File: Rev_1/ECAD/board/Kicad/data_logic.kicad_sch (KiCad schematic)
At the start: 5 parts

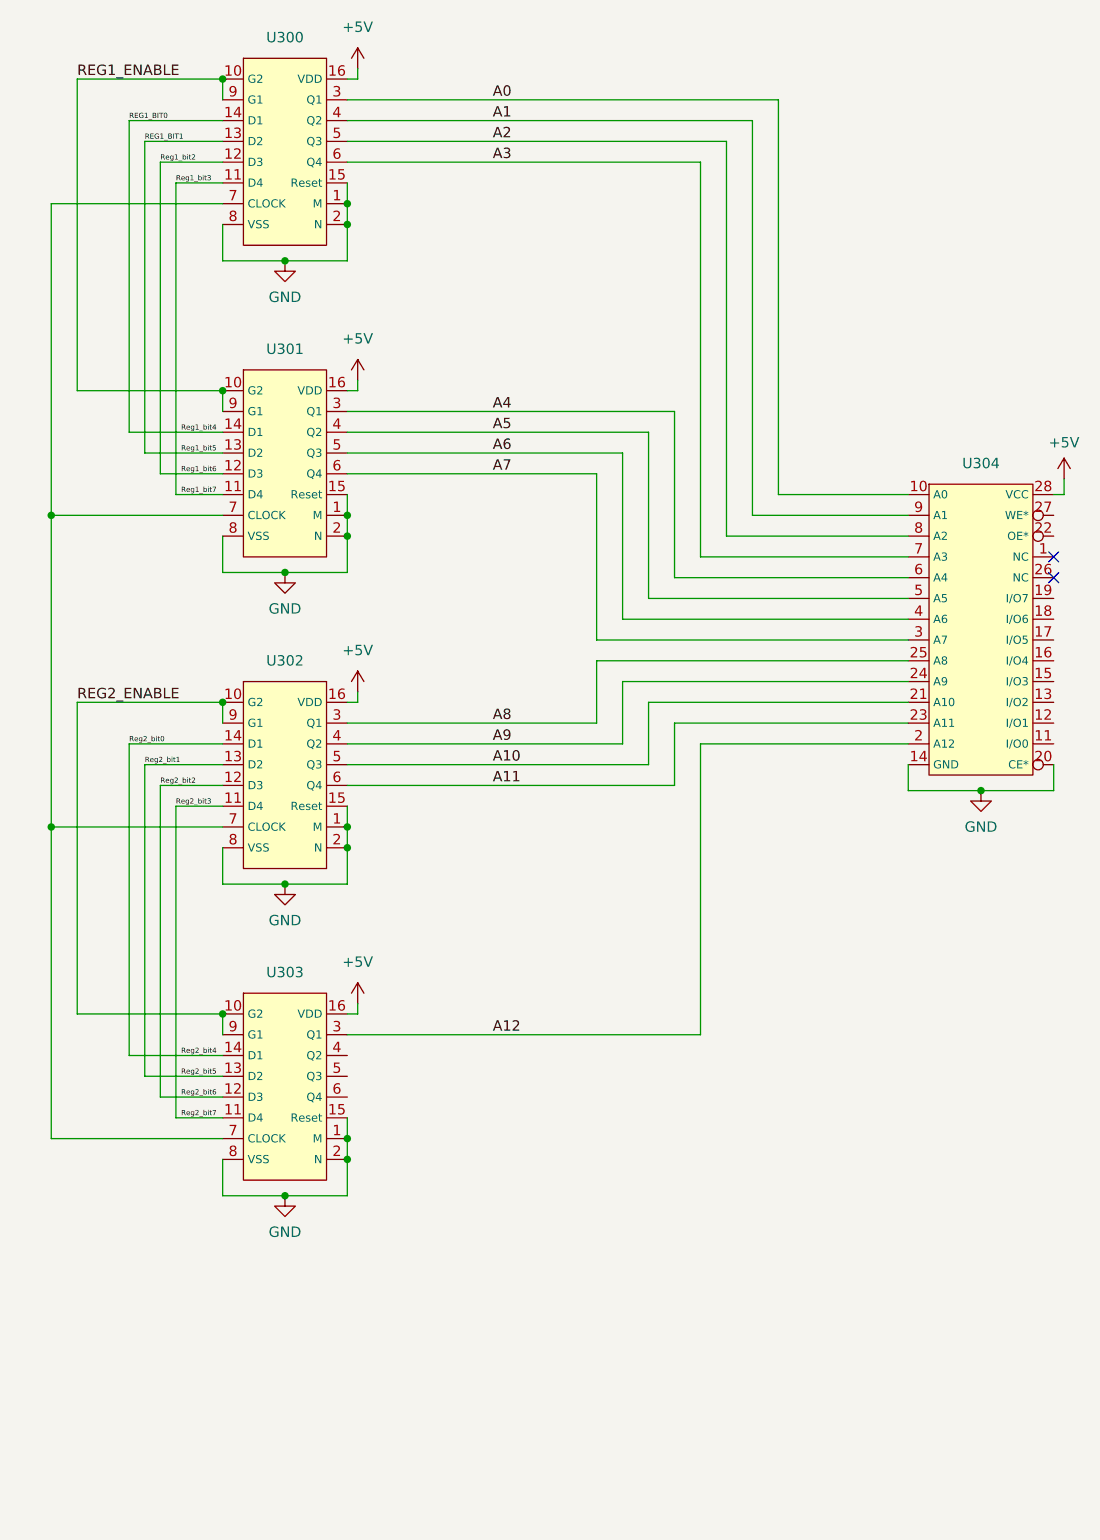
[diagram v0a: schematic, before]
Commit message: Updated net-name on Data Logic sheet
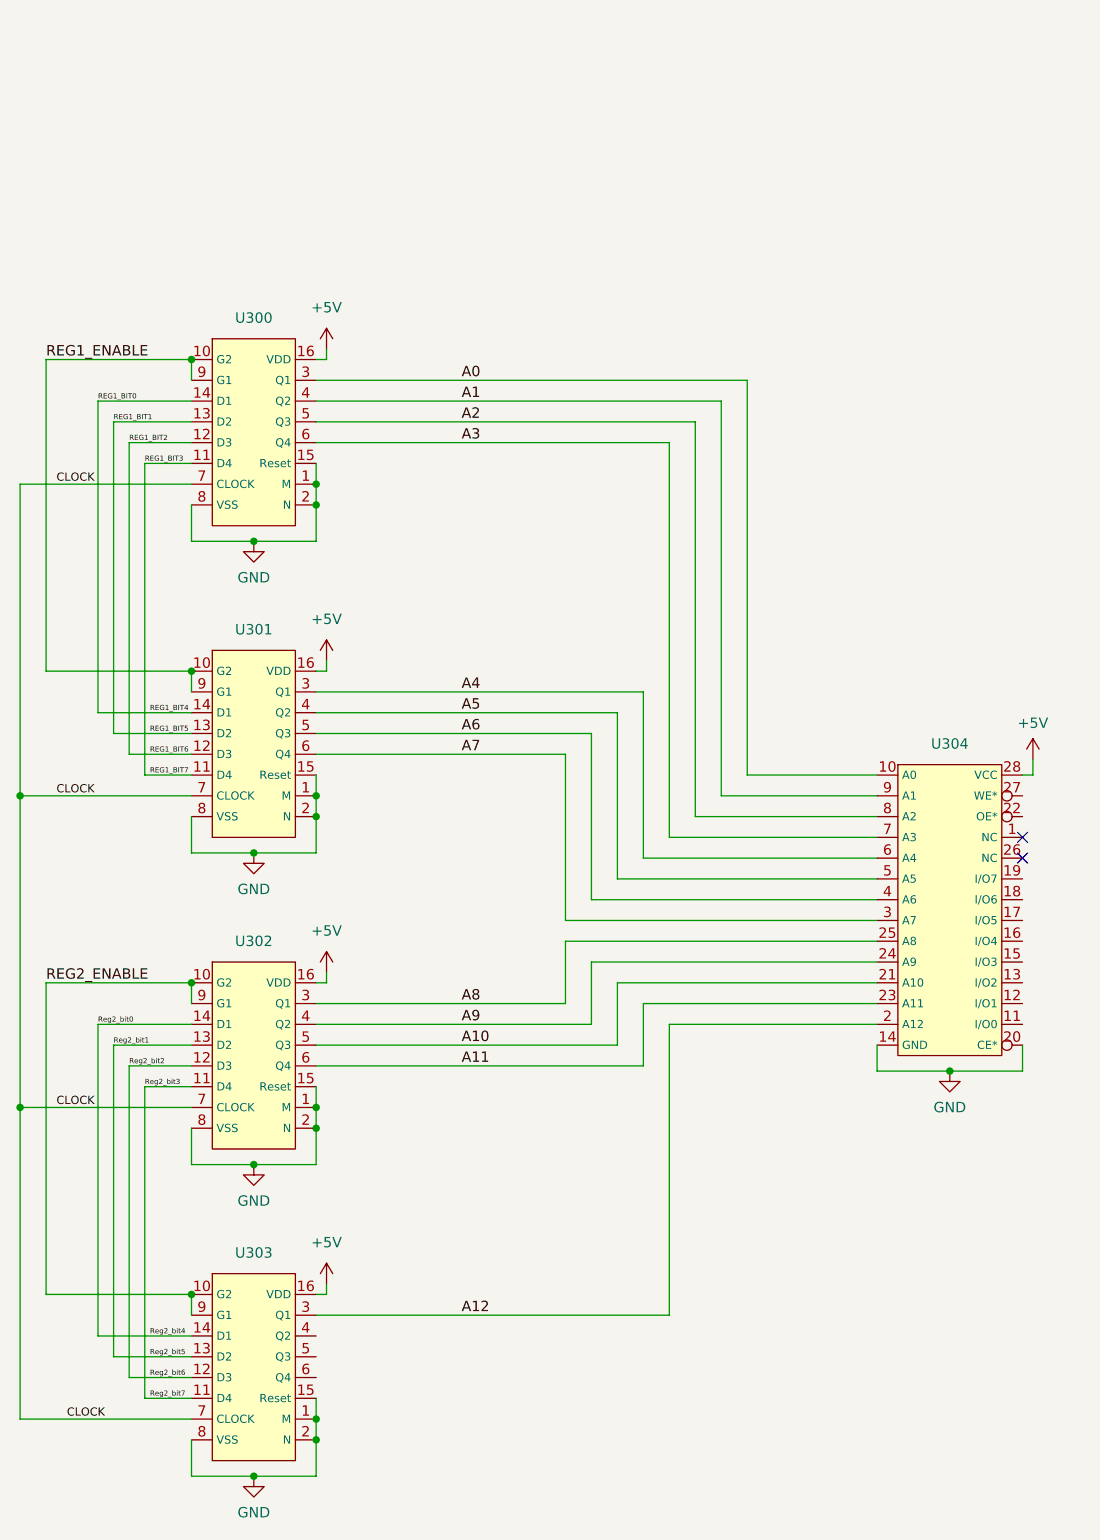
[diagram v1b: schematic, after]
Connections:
- net CLOCK: now reaches U300.7 (CLOCK), U301.7 (CLOCK), U302.7 (CLOCK), U303.7 (CLOCK)
- net Reg1_bit2 renamed REG1_BIT2
- net Reg1_bit3 renamed REG1_BIT3
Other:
- moved on the sheet: U300, U301, U302, U303, U304

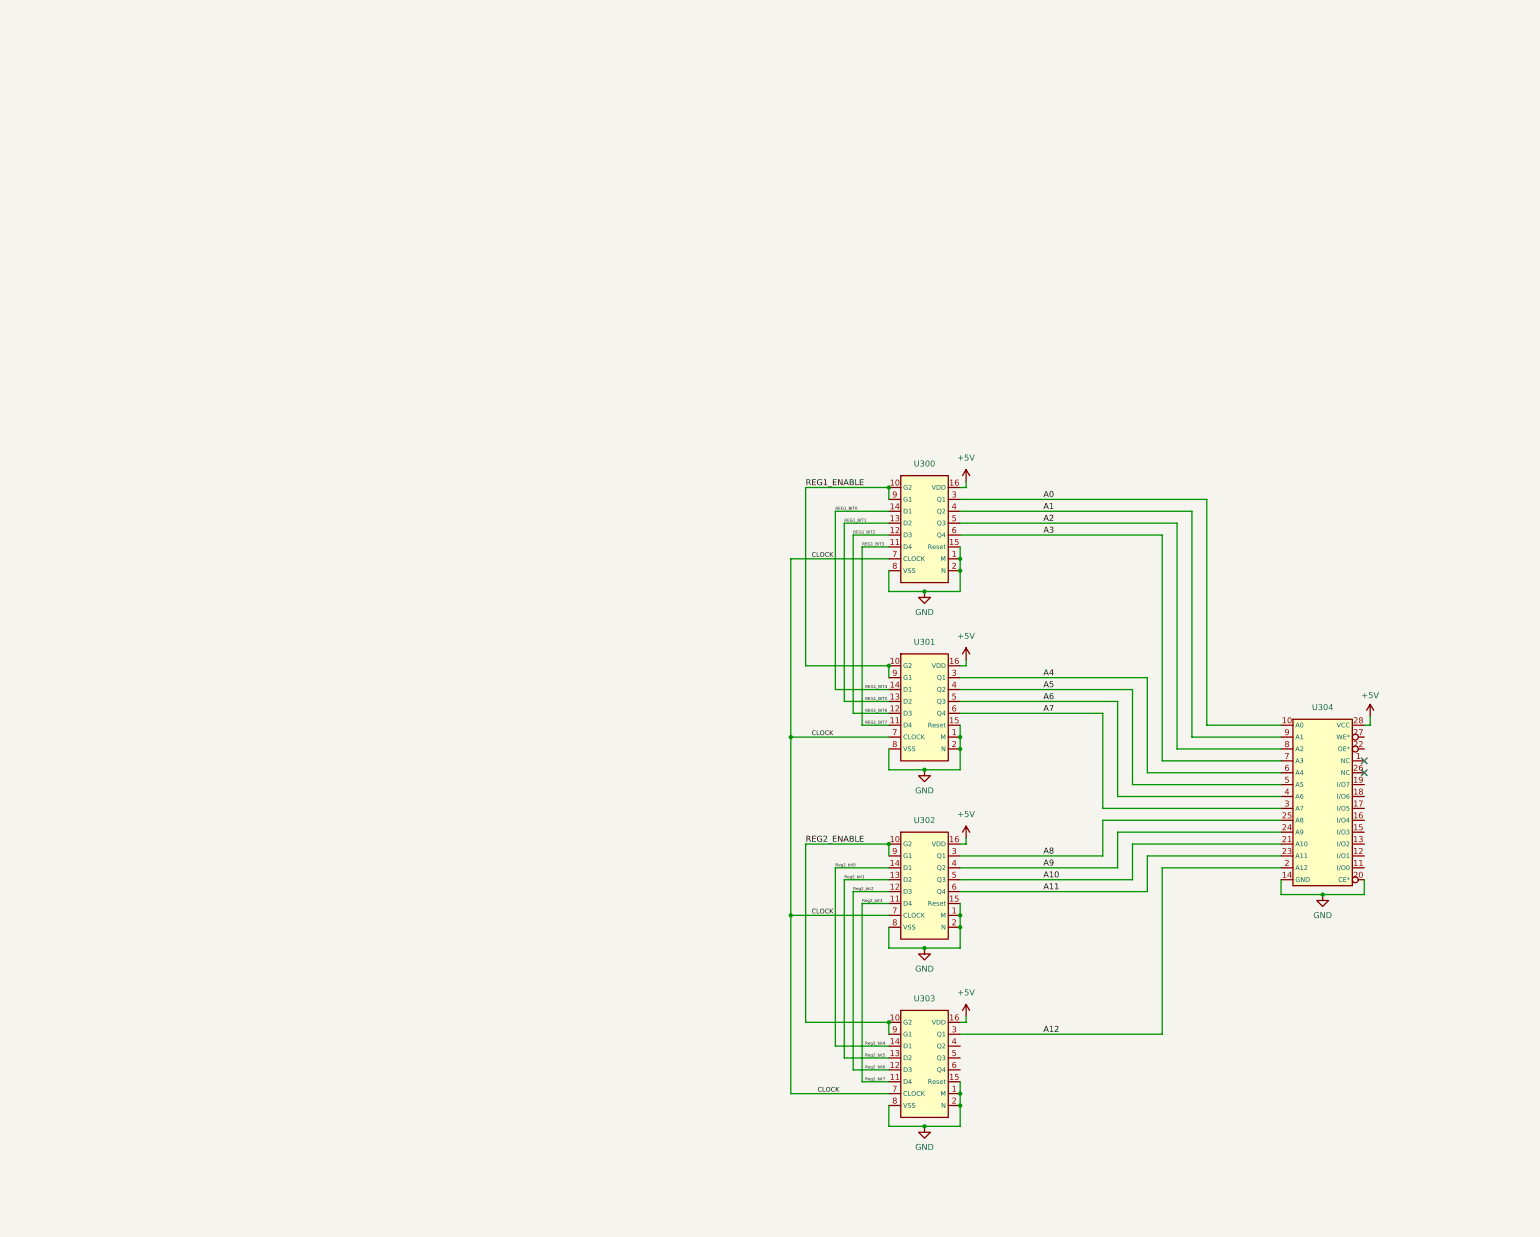
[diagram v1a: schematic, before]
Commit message: Added Bus aswell as data logic for the eeprom
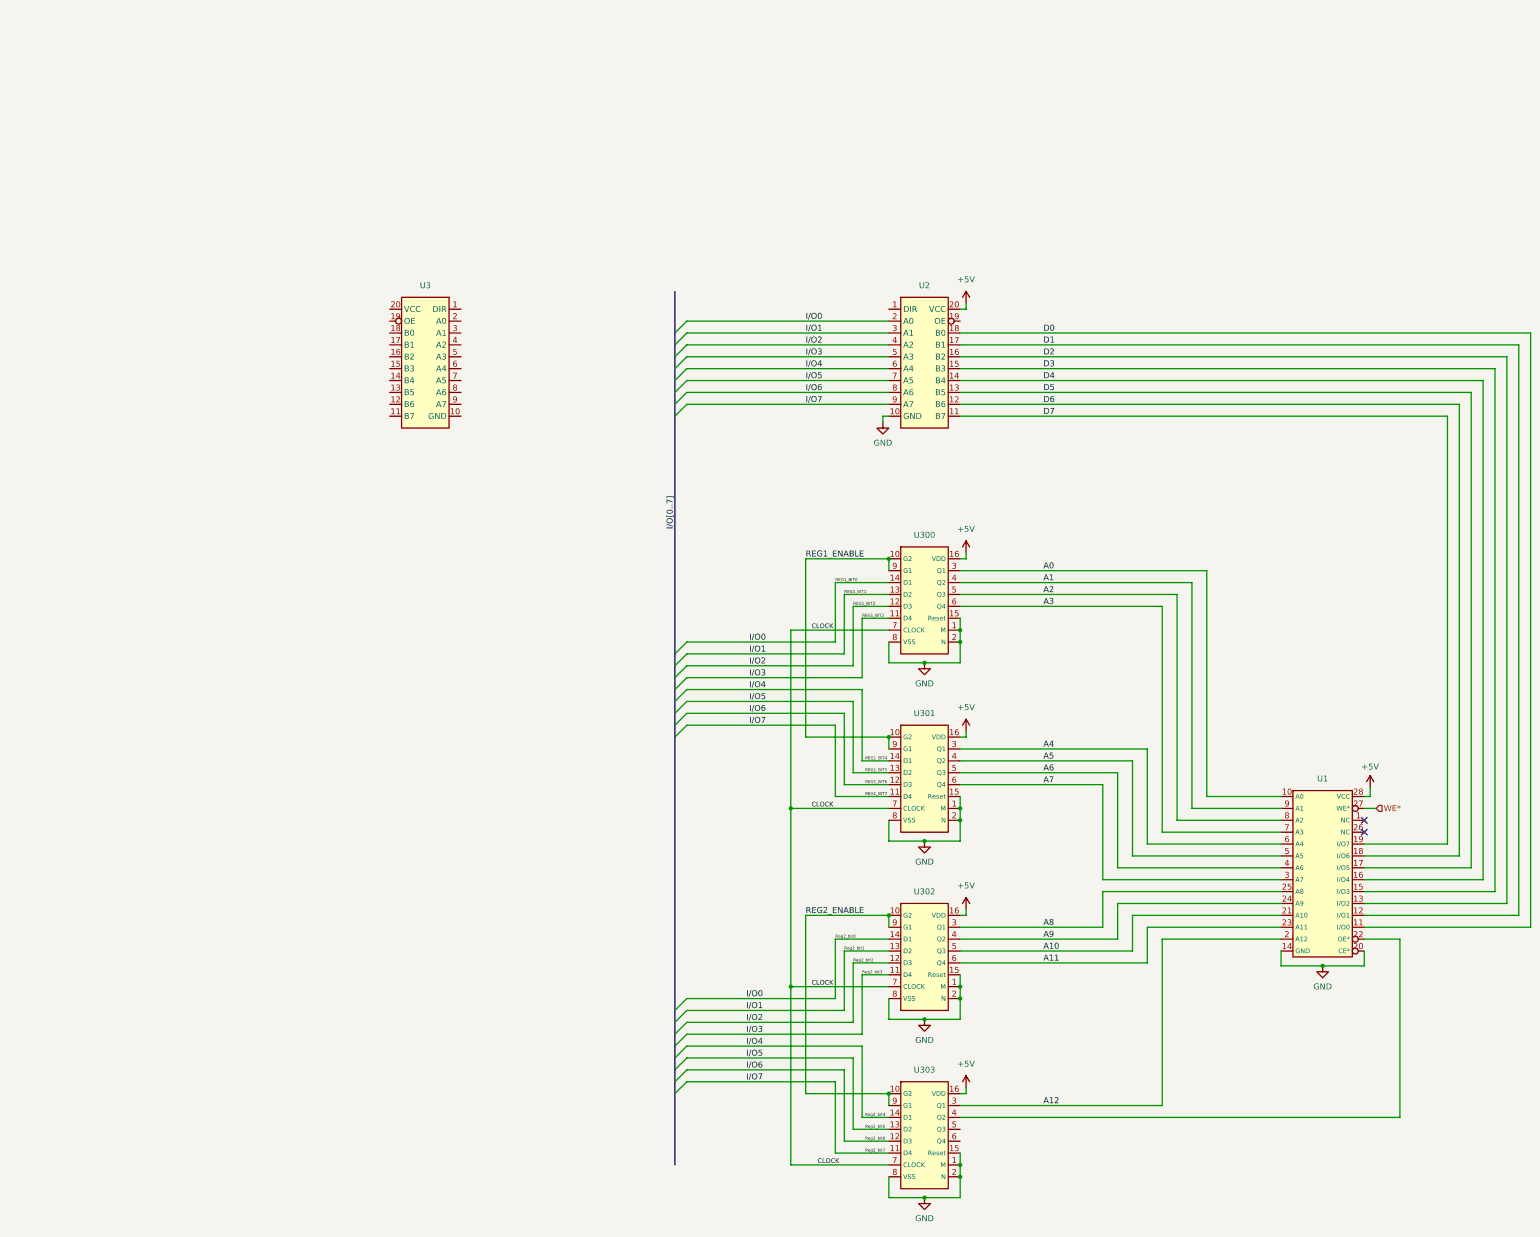
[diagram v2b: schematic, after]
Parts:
- removed U304: ~, symbol EEPROM_PROGRAMMER:AT28C64B-15PU
- added U1: ~, symbol EEPROM_PROGRAMER:AT28C64B-15PU
- added U2, U3: ~, symbol EEPROM_PROGRAMER:74HC245
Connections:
- net +5V: now also U1.28 (VCC), U2.20 (VCC)
- net A0: now also U1.10 (A0)
- net A1: now also U1.9 (A1)
- net A10: now also U1.21 (A10)
- net A11: now also U1.23 (A11)
- net A12: now also U1.2 (A12)
- net A2: now also U1.8 (A2)
- net A3: now also U1.7 (A3)
- net A4: now also U1.6 (A4)
- net A5: now also U1.5 (A5)
- net A6: now also U1.4 (A6)
- net A7: now also U1.3 (A7)
- net A8: now also U1.25 (A8)
- net A9: now also U1.24 (A9)
- net GND: now also U1.14 (GND), U1.20 (CE*), U2.10 (GND)
- net at U303.4 (Q2): now also U1.22 (OE*)
- net REG1_BIT0 renamed I/O0
- net I/O0: now also U302.14 (D1), U2.2 (A0); no longer U301.14 (D1)
- net REG1_BIT1 renamed I/O1
- net I/O1: now also U302.13 (D2), U2.3 (A1); no longer U301.13 (D2)
- net REG1_BIT2 renamed I/O2
- net I/O2: now also U302.12 (D3), U2.4 (A2); no longer U301.12 (D3)
- net REG1_BIT3 renamed I/O3
- net I/O3: now also U302.11 (D4), U2.5 (A3); no longer U301.11 (D4)
- net Reg2_bit0 renamed I/O4
- net I/O4: now also U301.14 (D1), U2.6 (A4); no longer U302.14 (D1)
- net Reg2_bit1 renamed I/O5
- net I/O5: now also U301.13 (D2), U2.7 (A5); no longer U302.13 (D2)
- net Reg2_bit2 renamed I/O6
- net I/O6: now also U301.12 (D3), U2.8 (A6); no longer U302.12 (D3)
- net Reg2_bit3 renamed I/O7
- net I/O7: now also U301.11 (D4), U2.9 (A7); no longer U302.11 (D4)
- new net D0: U1.11 (I/O0), U2.18 (B0)
- new net D1: U1.12 (I/O1), U2.17 (B1)
- new net D2: U1.13 (I/O2), U2.16 (B2)
- new net D3: U1.15 (I/O3), U2.15 (B3)
- new net D4: U1.16 (I/O4), U2.14 (B4)
- new net D5: U1.17 (I/O5), U2.13 (B5)
- new net D6: U1.18 (I/O6), U2.12 (B6)
- new net D7: U1.19 (I/O7), U2.11 (B7)
- new net WE*: U1.27 (WE*)
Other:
- moved on the sheet: U300, U301, U302, U303
